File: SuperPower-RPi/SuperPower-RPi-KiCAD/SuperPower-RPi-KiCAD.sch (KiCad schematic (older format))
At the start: 5 parts

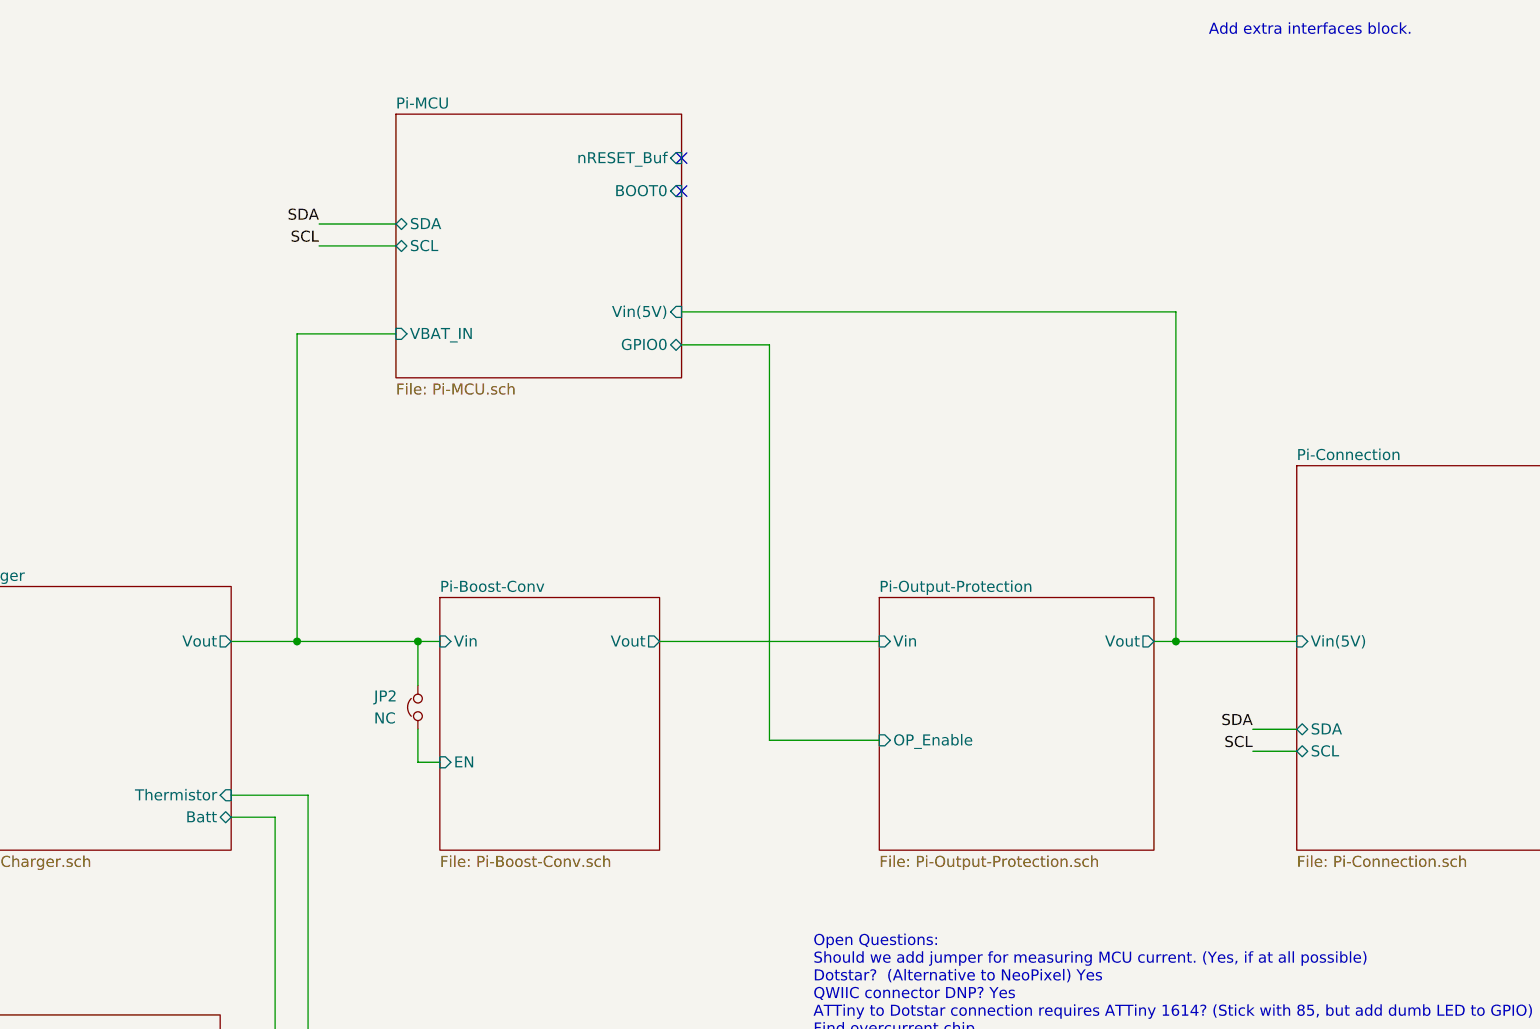
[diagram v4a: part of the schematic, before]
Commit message: Made connections between Pi and MCU, and cleared up some ERC errors.
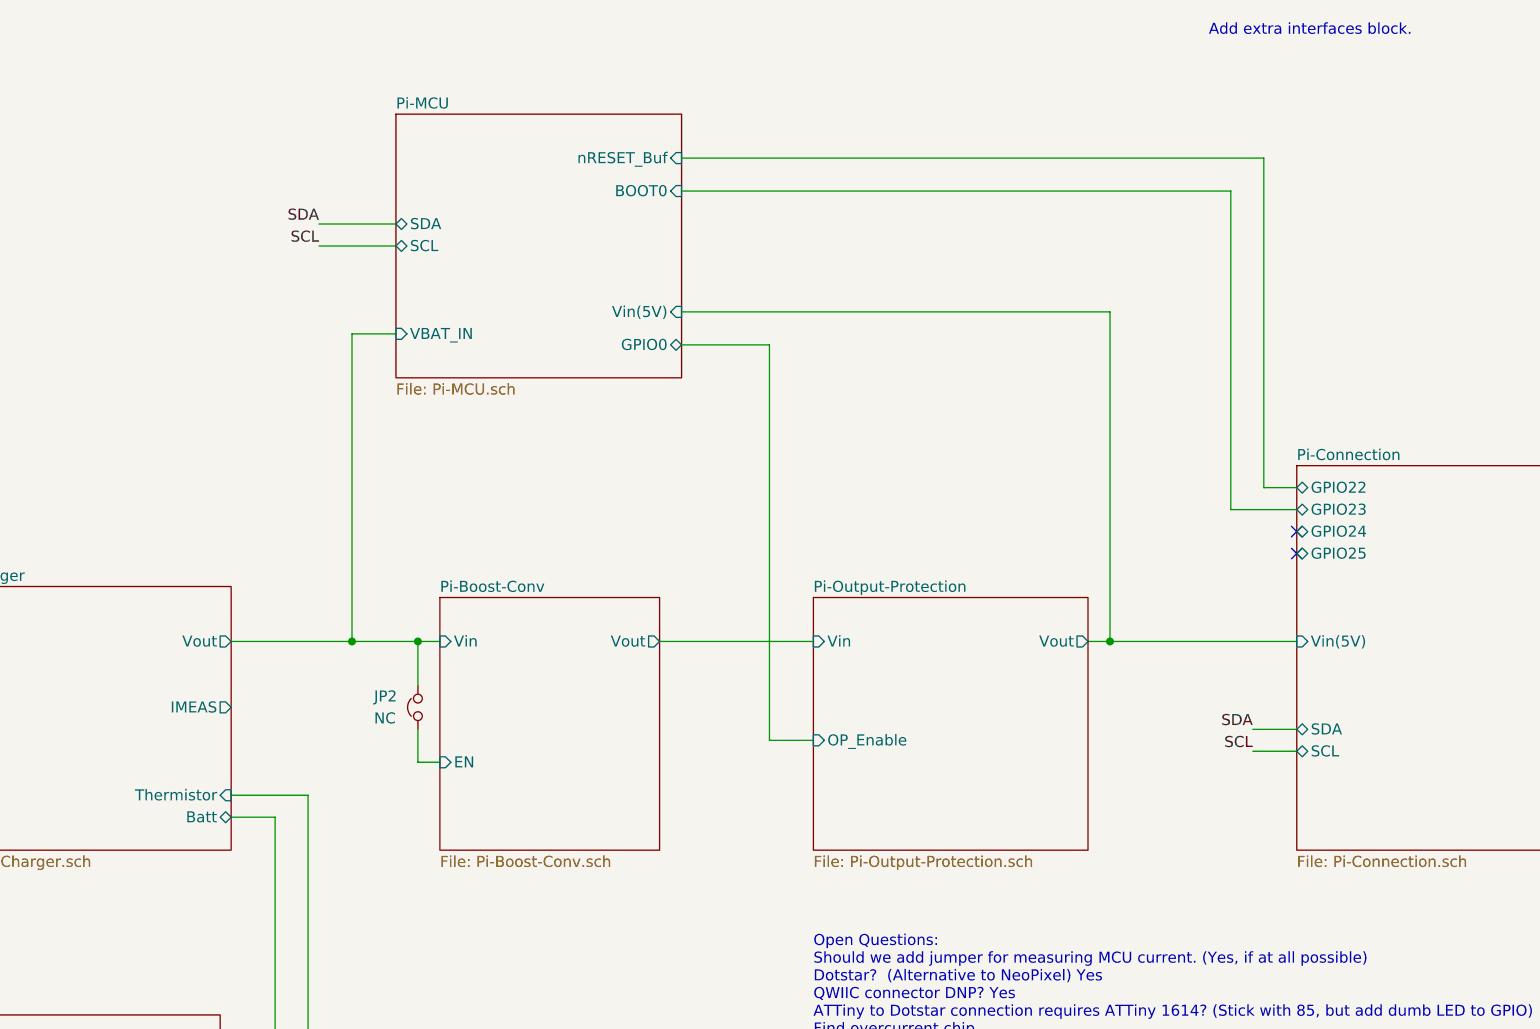
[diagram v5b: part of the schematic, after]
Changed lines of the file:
@@
 $EndDescr
 Wire Wire Line
-	6950 4100 7450 4100
+	6950 4100 7150 4100
 Wire Wire Line
 	6550 2300 6950 2300
@@
 	3200 4400 2950 4400
 Wire Wire Line
-	8700 3650 8800 3650
-Wire Wire Line
-	6450 3650 7450 3650
+	8400 3650 8500 3650
+Wire Wire Line
+	6450 3650 7150 3650
 Wire Wire Line
 	2300 3650 3200 3650
 Wire Wire Line
-	4500 3650 4800 3650
+	4500 3650 5050 3650
 $Sheet
 S 5450 3450 1000 1150
@@
 $EndSheet
 $Sheet
-S 7450 3450 1250 1150
+S 7150 3450 1250 1150
 U 5F6AC517
 F0 "Pi-Output-Protection" 50
 F1 "Pi-Output-Protection.sch" 50
-F2 "Vin" I L 7450 3650 50
-F3 "Vout" O R 8700 3650 50
-F4 "OP_Enable" I L 7450 4100 50
+F2 "Vin" I L 7150 3650 50
+F3 "Vout" O R 8400 3650 50
+F4 "OP_Enable" I L 7150 4100 50
 $EndSheet
 $Sheet
@@
 F8 "D+" I L 3200 3950 50
 F9 "D-" I L 3200 4050 50
+F10 "IMEAS" O R 4500 3950 50
 $EndSheet
 Wire Wire Line
@@
 Add extra interfaces block.
 Wire Wire Line
-	5250 2250 4800 2250
-Connection ~ 4800 3650
-Wire Wire Line
-	4800 2250 4800 3650
+	5250 2250 5050 2250
+Connection ~ 5050 3650
+Wire Wire Line
+	5050 2250 5050 3650
 $Comp
 L Mechanical:MountingHole H1
@@
 	1    0    0    -1
 $EndComp
-NoConn ~ 6550 1450
-NoConn ~ 6550 1600
 $Sheet
 S 5250 1250 1300 1200
@@
 $EndSheet
 Wire Wire Line
-	6550 2150 8800 2150
+	6550 2150 8500 2150
 Wire Wire Line
 	5450 4200 5350 4200
@@
 	5350 3650 5450 3650
 Wire Wire Line
-	4800 3650 5350 3650
+	5050 3650 5350 3650
 Connection ~ 5350 3650
 Wire Wire Line
@@
 	6950 2300 6950 4100
 Wire Wire Line
-	8800 2150 8800 3650
+	8500 2150 8500 3650
 Text Notes 7150 5450 0    50   ~ 0
 Open Questions:\nShould we add jumper for measuring MCU current. (Yes, if at all possible)\nDotstar?  (Alternative to NeoPixel) Yes\nQWIIC connector DNP? Yes\nATTiny to Dotstar connection requires ATTiny 1614? (Stick with 85, but add dumb LED to GPIO)\nFind overcurrent chip
+Connection ~ 8500 3650
+Wire Wire Line
+	8500 3650 9350 3650
+Text Notes 7150 5800 0    50   ~ 0
+Would be nice:\nUSB output connector to power \nAdd QWIIC to mulitple I2C busses\n
+Text Notes 7150 6100 0    50   ~ 0
+TO DO:\nMove primary I2C to I2C1.\nAdd dumb LED to ATTiny
+Wire Wire Line
+	6550 1450 9200 1450
+Wire Wire Line
+	9200 1450 9200 2950
+Wire Wire Line
+	9200 2950 9350 2950
+Wire Wire Line
+	9350 3050 9050 3050
+Wire Wire Line
+	9050 3050 9050 1600
+Wire Wire Line
+	9050 1600 6550 1600
 $Sheet
 S 9350 2850 1350 1750
@@
 F3 "SDA" B L 9350 4050 50
 F4 "SCL" B L 9350 4150 50
-$EndSheet
-Connection ~ 8800 3650
-Wire Wire Line
-	8800 3650 9350 3650
-Text Notes 7150 5800 0    50   ~ 0
-Would be nice:\nUSB output connector to power \nAdd QWIIC to mulitple I2C busses\n
-Text Notes 7150 6100 0    50   ~ 0
-TO DO:\nMove primary I2C to I2C1.\nAdd dumb LED to ATTiny
+F5 "GPIO22" B L 9350 2950 50
+F6 "GPIO23" B L 9350 3050 50
+F7 "GPIO24" B L 9350 3150 50
+F8 "GPIO25" B L 9350 3250 50
+$EndSheet
+NoConn ~ 9350 3250
+NoConn ~ 9350 3150
 $EndSCHEMATC

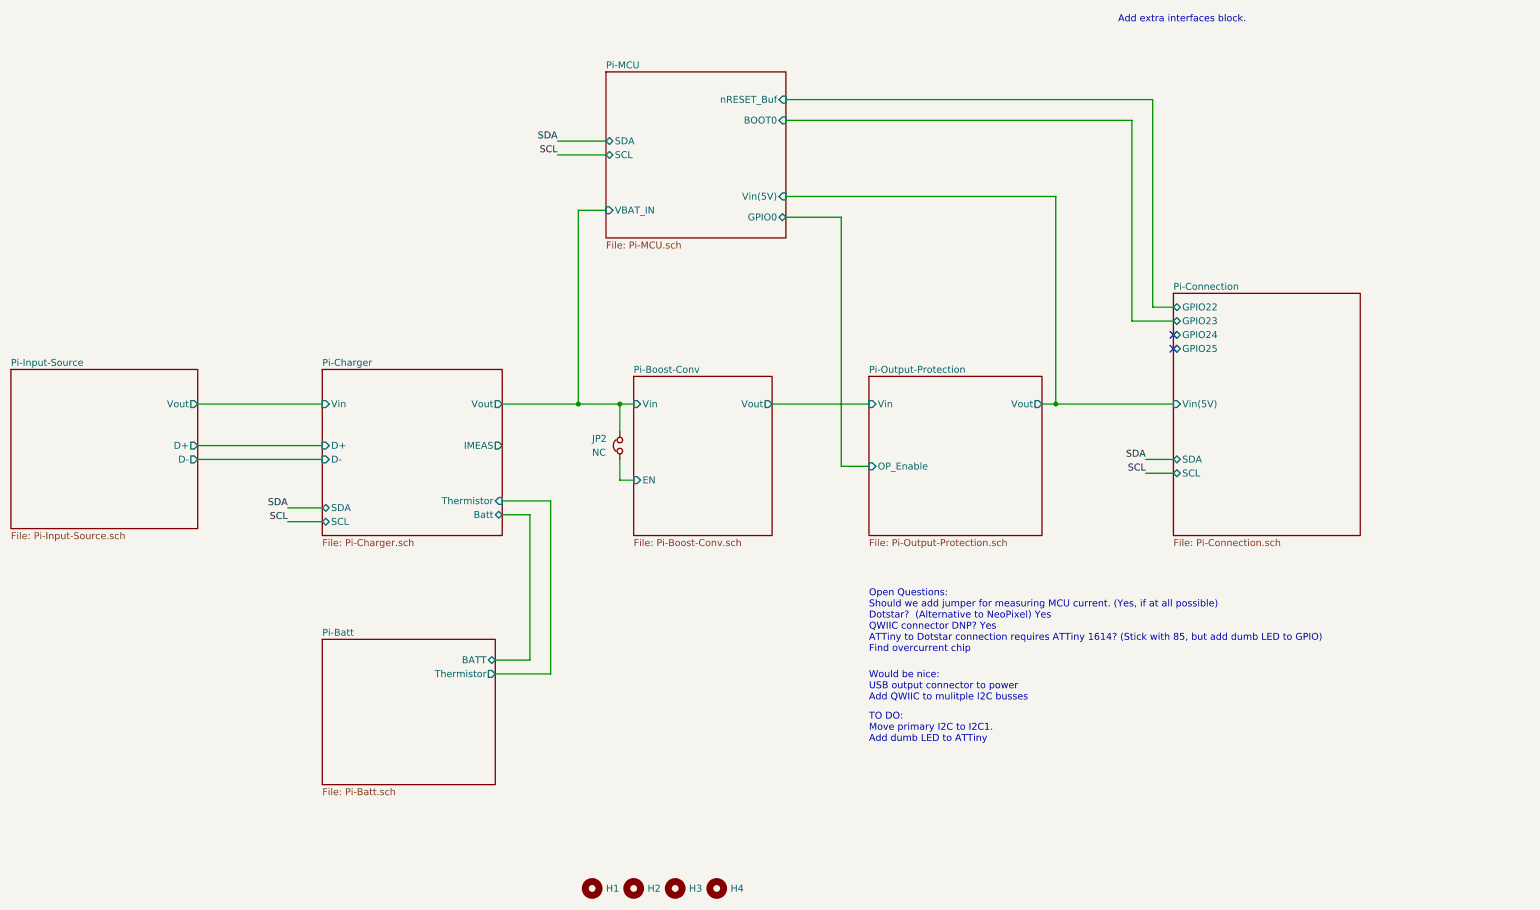
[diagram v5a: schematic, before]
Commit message: Added Jumper to MCU power, and made I2c changes.
Moved all the main I2C connections to the STMs I2C1 Port.  Also added a spare QWIIC/Stemma connection on I2C3.
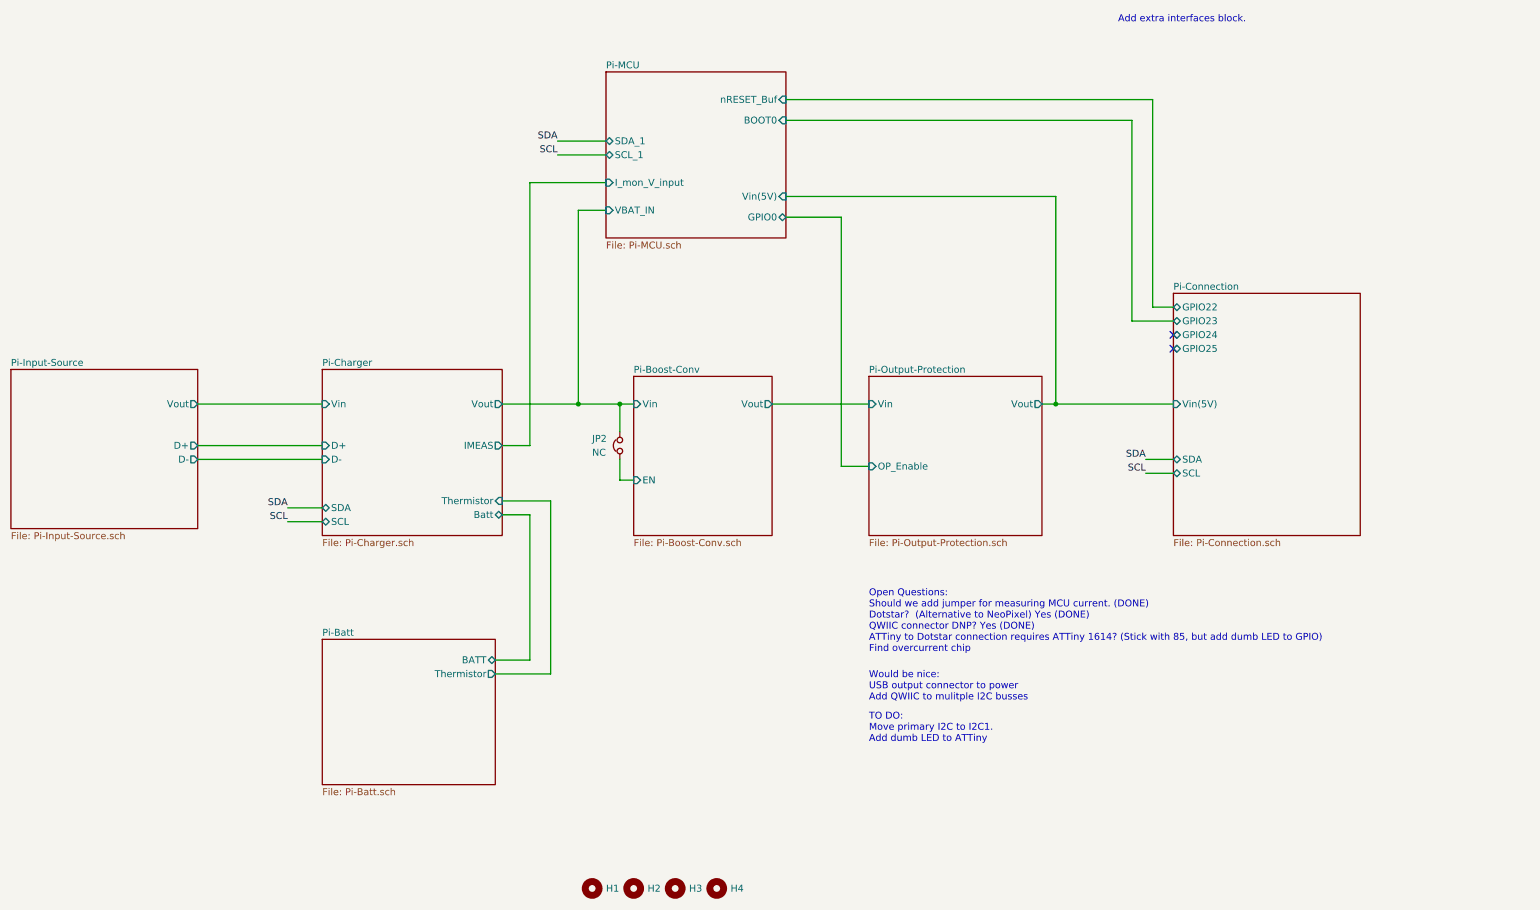
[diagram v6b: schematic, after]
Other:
- note added: "Open Questions:\nShould we add jumper for measuring MCU current. (DONE)\nDotstar? (Alternative to NeoPixel) Yes (DONE)\nQWIIC connector DNP? Yes (DONE)\nATTiny to Dotstar connection requires ATTiny 1614? (Stick with 85, but add dumb LED to GPIO)\nFind overcurrent chip"
- note removed: "Open Questions:\nShould we add jumper for measuring MCU current. (Yes, if at all possible)\nDotstar? (Alternative to NeoPixel) Yes\nQWIIC connector DNP? Yes\nATTiny to Dotstar connection requires ATTiny 1614? (Stick with 85, but add dumb LED to GPIO)\nFind overcurrent chip"
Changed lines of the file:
@@
 F0 "Pi-MCU" 50
 F1 "Pi-MCU.sch" 50
-F2 "SDA" B L 5250 1750 50
-F3 "SCL" B L 5250 1850 50
+F2 "SDA_1" B L 5250 1750 50
+F3 "SCL_1" B L 5250 1850 50
 F4 "GPIO0" B R 6550 2300 50
 F5 "VBAT_IN" I L 5250 2250 50
@@
 F7 "BOOT0" I R 6550 1600 50
 F8 "Vin(5V)" I R 6550 2150 50
+F9 "I_mon_V_input" I L 5250 2050 50
 $EndSheet
 Wire Wire Line
@@
 	8500 2150 8500 3650
 Text Notes 7150 5450 0    50   ~ 0
-Open Questions:\nShould we add jumper for measuring MCU current. (Yes, if at all possible)\nDotstar?  (Alternative to NeoPixel) Yes\nQWIIC connector DNP? Yes\nATTiny to Dotstar connection requires ATTiny 1614? (Stick with 85, but add dumb LED to GPIO)\nFind overcurrent chip
+Open Questions:\nShould we add jumper for measuring MCU current. (DONE)\nDotstar?  (Alternative to NeoPixel) Yes (DONE)\nQWIIC connector DNP? Yes (DONE)\nATTiny to Dotstar connection requires ATTiny 1614? (Stick with 85, but add dumb LED to GPIO)\nFind overcurrent chip
 Connection ~ 8500 3650
 Wire Wire Line
@@
 NoConn ~ 9350 3250
 NoConn ~ 9350 3150
+Wire Wire Line
+	5250 2050 4700 2050
+Wire Wire Line
+	4700 2050 4700 3950
+Wire Wire Line
+	4700 3950 4500 3950
 $EndSCHEMATC

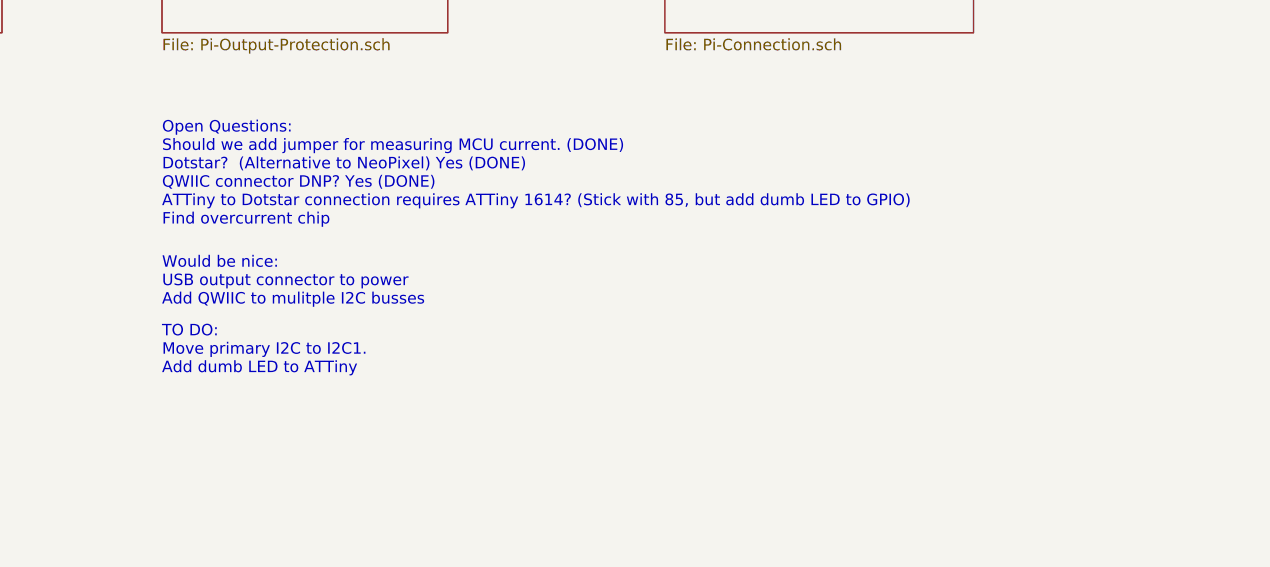
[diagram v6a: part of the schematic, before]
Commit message: Fixed ERC errors.
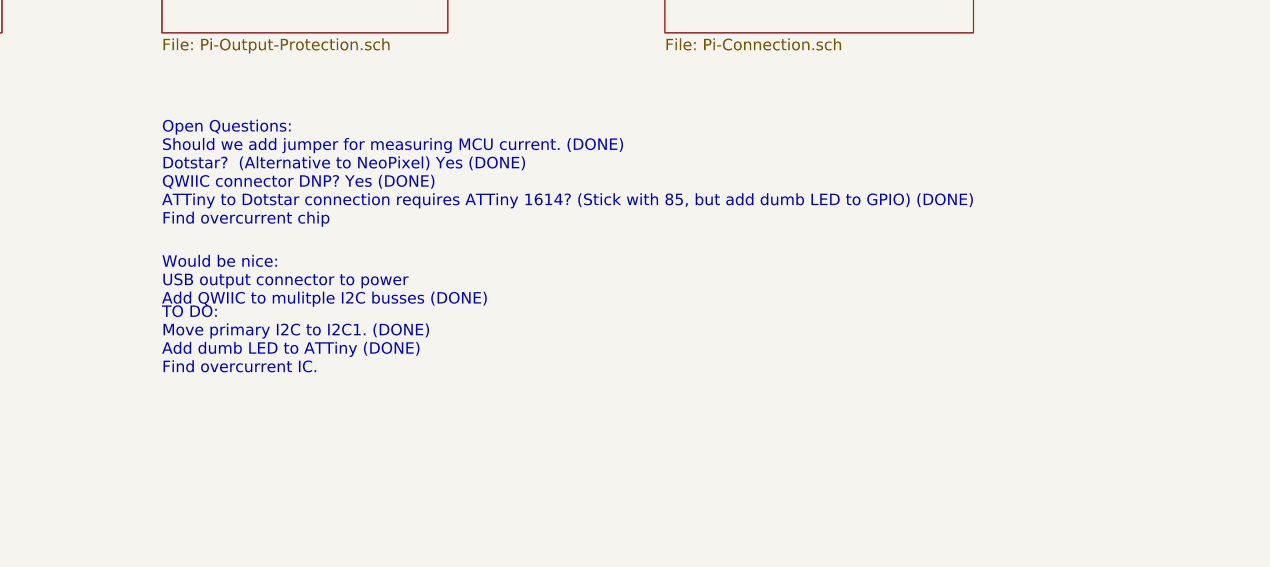
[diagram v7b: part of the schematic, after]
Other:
- note added: "Open Questions:\nShould we add jumper for measuring MCU current. (DONE)\nDotstar? (Alternative to NeoPixel) Yes (DONE)\nQWIIC connector DNP? Yes (DONE)\nATTiny to Dotstar connection requires ATTiny 1614? (Stick with 85, but add dumb LED to GPIO) (DONE)\nFind overcurrent chip"
- note added: "TO DO:\nMove primary I2C to I2C1. (DONE)\nAdd dumb LED to ATTiny (DONE)\nFind overcurrent IC."
- note added: "Would be nice:\nUSB output connector to power \nAdd QWIIC to mulitple I2C busses (DONE)\n"
- note removed: "Open Questions:\nShould we add jumper for measuring MCU current. (DONE)\nDotstar? (Alternative to NeoPixel) Yes (DONE)\nQWIIC connector DNP? Yes (DONE)\nATTiny to Dotstar connection requires ATTiny 1614? (Stick with 85, but add dumb LED to GPIO)\nFind overcurrent chip"
- note removed: "TO DO:\nMove primary I2C to I2C1.\nAdd dumb LED to ATTiny"
- note removed: "Would be nice:\nUSB output connector to power \nAdd QWIIC to mulitple I2C busses\n"
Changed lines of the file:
@@
 	8500 2150 8500 3650
 Text Notes 7150 5450 0    50   ~ 0
-Open Questions:\nShould we add jumper for measuring MCU current. (DONE)\nDotstar?  (Alternative to NeoPixel) Yes (DONE)\nQWIIC connector DNP? Yes (DONE)\nATTiny to Dotstar connection requires ATTiny 1614? (Stick with 85, but add dumb LED to GPIO)\nFind overcurrent chip
+Open Questions:\nShould we add jumper for measuring MCU current. (DONE)\nDotstar?  (Alternative to NeoPixel) Yes (DONE)\nQWIIC connector DNP? Yes (DONE)\nATTiny to Dotstar connection requires ATTiny 1614? (Stick with 85, but add dumb LED to GPIO) (DONE)\nFind overcurrent chip
 Connection ~ 8500 3650
 Wire Wire Line
 	8500 3650 9350 3650
 Text Notes 7150 5800 0    50   ~ 0
-Would be nice:\nUSB output connector to power \nAdd QWIIC to mulitple I2C busses\n
+Would be nice:\nUSB output connector to power \nAdd QWIIC to mulitple I2C busses (DONE)\n
 Text Notes 7150 6100 0    50   ~ 0
-TO DO:\nMove primary I2C to I2C1.\nAdd dumb LED to ATTiny
+TO DO:\nMove primary I2C to I2C1. (DONE)\nAdd dumb LED to ATTiny (DONE)\nFind overcurrent IC.
 Wire Wire Line
 	6550 1450 9200 1450
